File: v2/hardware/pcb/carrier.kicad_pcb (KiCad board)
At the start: 2 copper layers, 91.2 x 91.2 mm, 20 parts, among them J1 12V IN (JST-XH), J2 I2C expansion (not fitted), U1 K7805-1000R3 / R-78E5.0-1.0, U2 ESP32-S3-Zero, U3 LD2412, U4 HC-SR602, U5 GY-302 BH1750, U6 ENS160+AHT21, U7 SCD40/SCD41 (option)

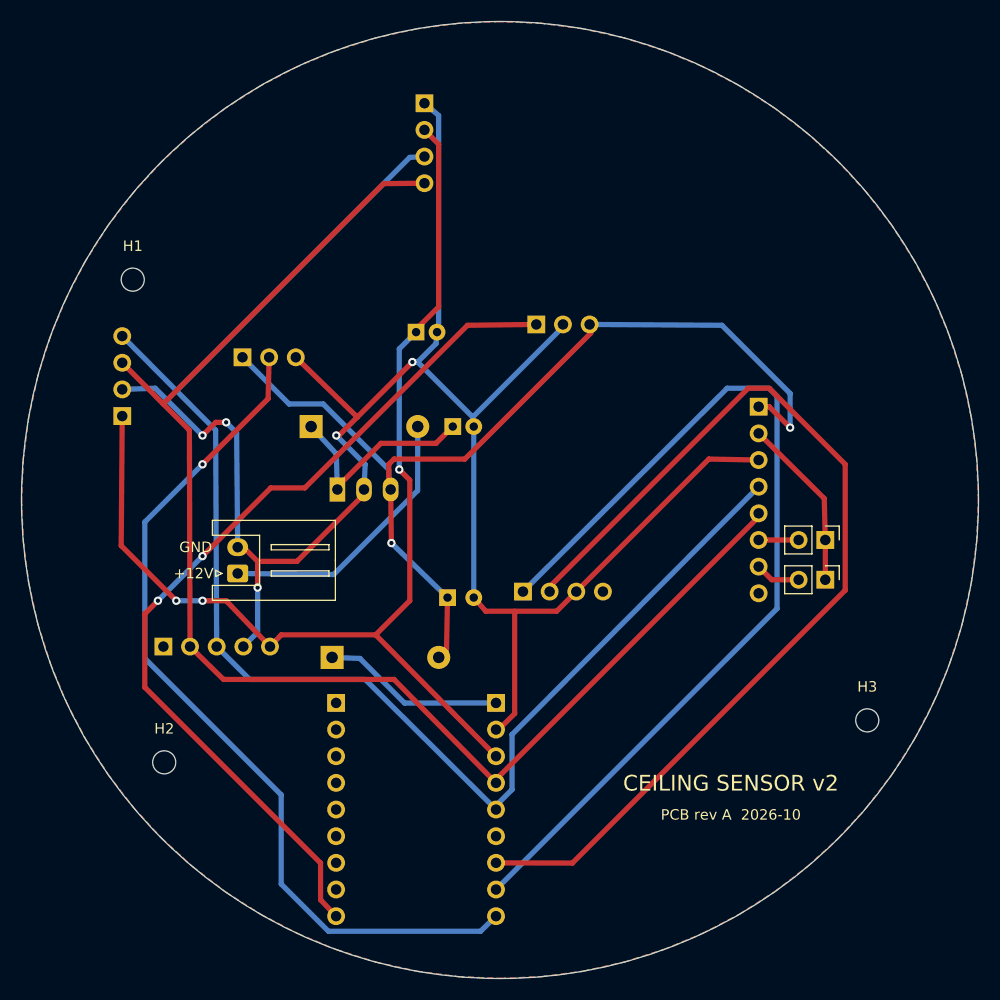
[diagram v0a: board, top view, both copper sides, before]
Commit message: v2: PIR socket pin order OUT, +, - (+ in the middle, as on the HW-438 board)
Co-Authored-By: Claude Opus 5.5 <noreply@anthropic.com>
Claude-Session: https://claude.ai/code/session_012hTjUXJJHKxpQwcsCnExu2
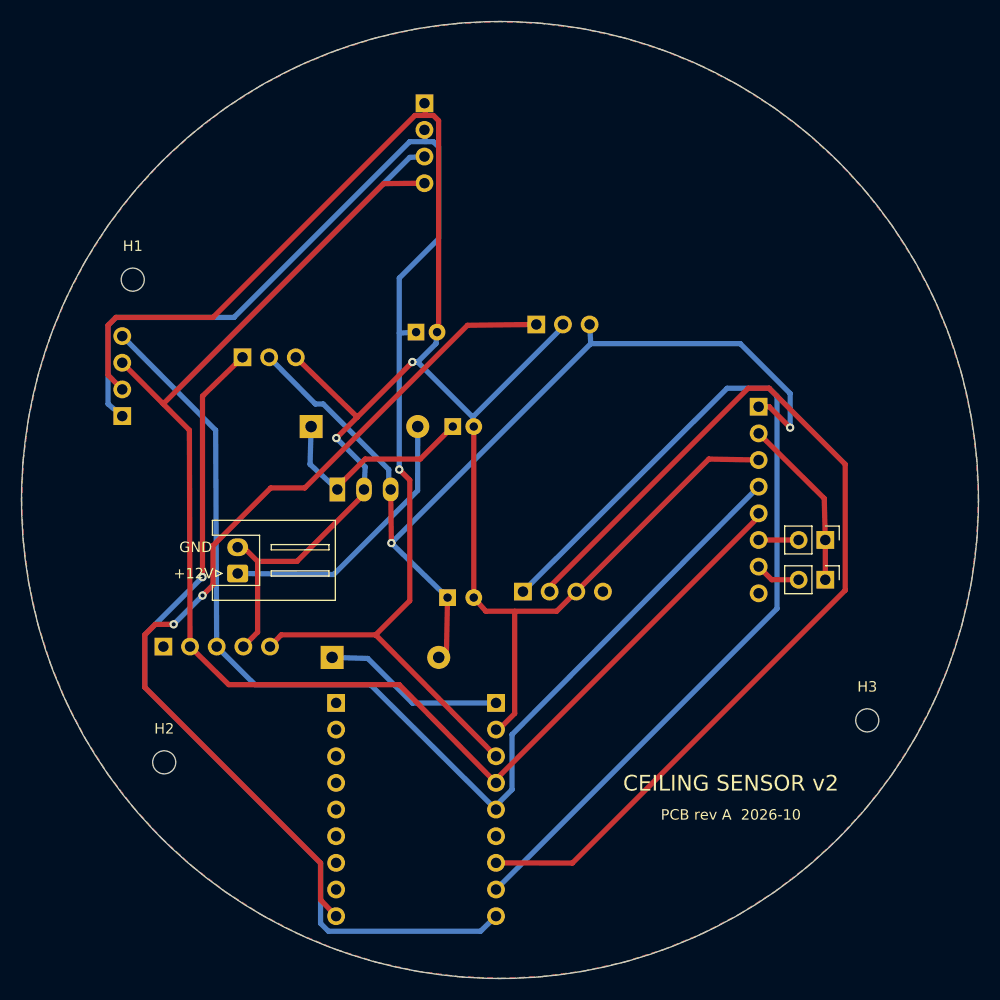
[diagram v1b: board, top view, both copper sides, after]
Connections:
- U4 pad 1: +5V -> PIR_OUT
- U4 pad 2: PIR_OUT -> +5V
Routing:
- net GND: track 183.1 -> 203.9 mm, vias 5 -> 2
- net +3V3: track 109.5 -> 127.6 mm, vias 3 -> 1
- net +5V: track 95.6 -> 93.2 mm
- net RADAR_OUT: track 85.0 -> 86.1 mm
- net PIR_OUT: track 83.4 -> 82.4 mm

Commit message: v2: separate SHT40 for room temperature/humidity in its own pocket
The AHT21 on the ENS160 combo board reads ~10 degC high on the prototype
(the ENS160 heater sits next to it). v2 adds a GY-SHT40 (U8) in a walled,
vented pocket with no copper pour above it; the AHT21 now only feeds the
ENS160 compensation and shows up as a diagnostic chamber temperature.

Co-Authored-By: Claude Opus 5.5 <noreply@anthropic.com>
Claude-Session: https://claude.ai/code/session_012hTjUXJJHKxpQwcsCnExu2
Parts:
- added CH2: SHT40 pocket walls (housing), ceiling_v2:PocketWalls, B.Cu at (125.5, 74.0)
- added U8: GY-SHT40, ceiling_v2:Module_SHT, B.Cu at (125.5, 74.0)
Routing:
- net RADAR_RX: track 95.6 -> 27.9 mm, vias 0 -> 1
- net RADAR_TX: track 90.6 -> 29.4 mm
- net SCL: track 140.2 -> 166.3 mm
- net SDA: track 133.8 -> 159.8 mm
- net PIR_OUT: track 82.4 -> 66.7 mm
- net +5V: track 93.2 -> 80.2 mm, vias 2 -> 1
- net +3V3: track 127.6 -> 138.7 mm, vias 1 -> 2
- net RADAR_OUT: track 86.1 -> 82.2 mm, vias 2 -> 0
- net VIN_RAW: track 26.6 -> 23.8 mm
- net GND: track 203.9 -> 205.4 mm, vias 2 -> 4
- net ENS_3V3: track 16.6 -> 18.1 mm, vias 0 -> 1
